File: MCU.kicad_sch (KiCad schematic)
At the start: 41 parts, among them IC9 ATSAMD21G18A-MF, J10 SAMTEC_SSW-106-01-L-S, J7 SAMTEC_SSW-108-01-G-S, J8 SAMTEC_SSW-110-01-G-S, J9 SAMTEC_SSW-108-01-G-S, Q1 XTAL_32.768KHZ_ABRACON_ABS09-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

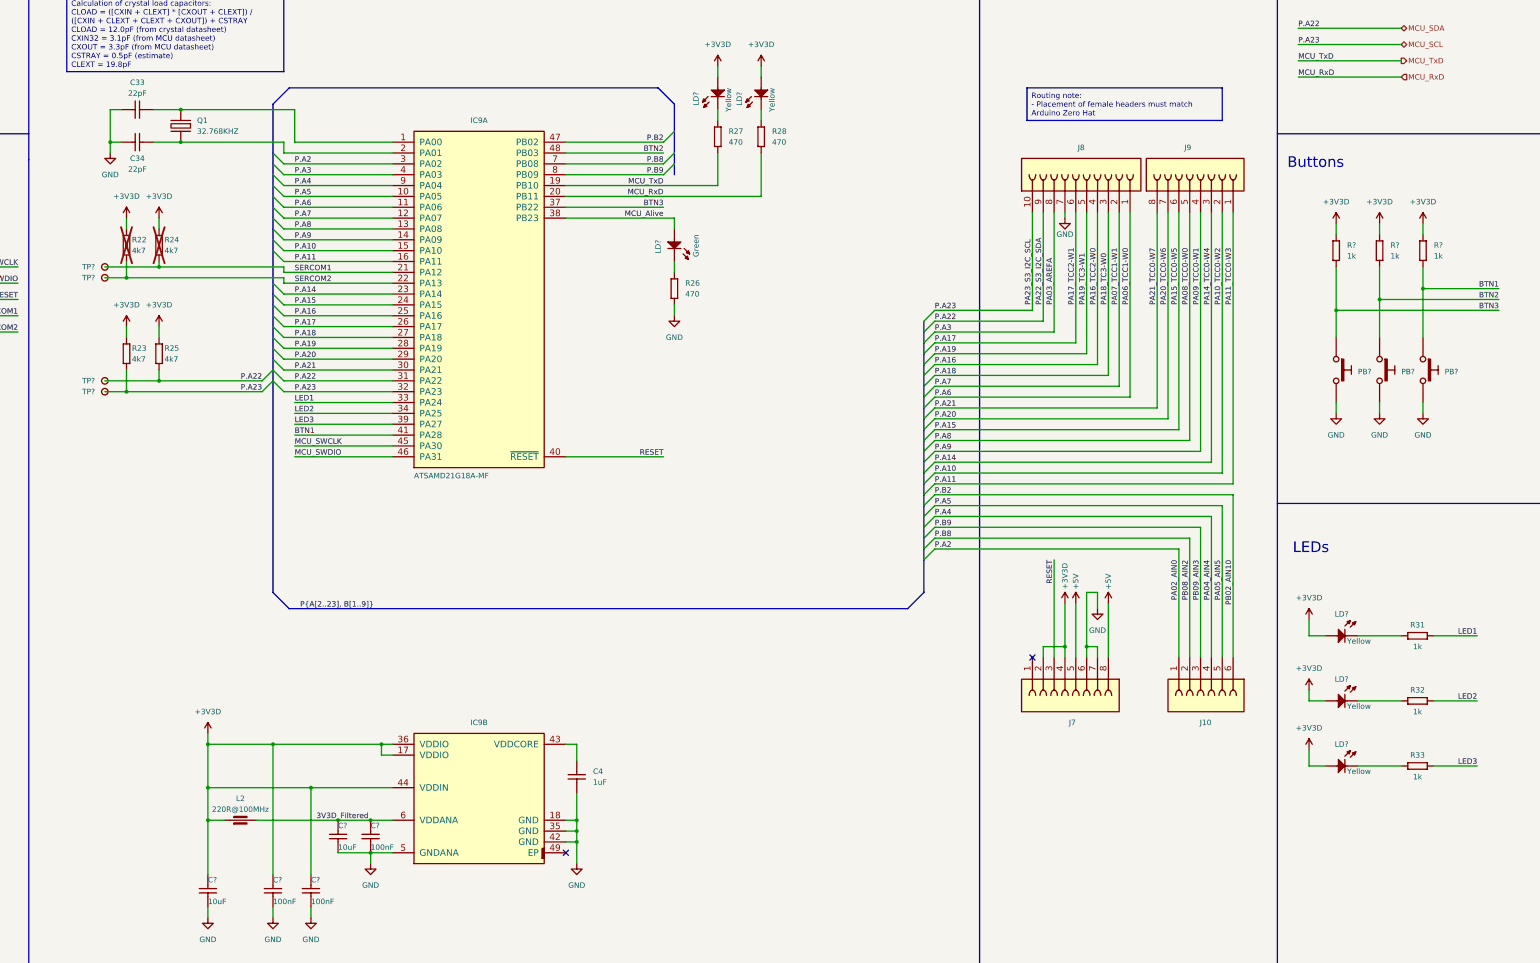
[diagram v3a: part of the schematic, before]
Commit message: Updated schematic after routing, added layout
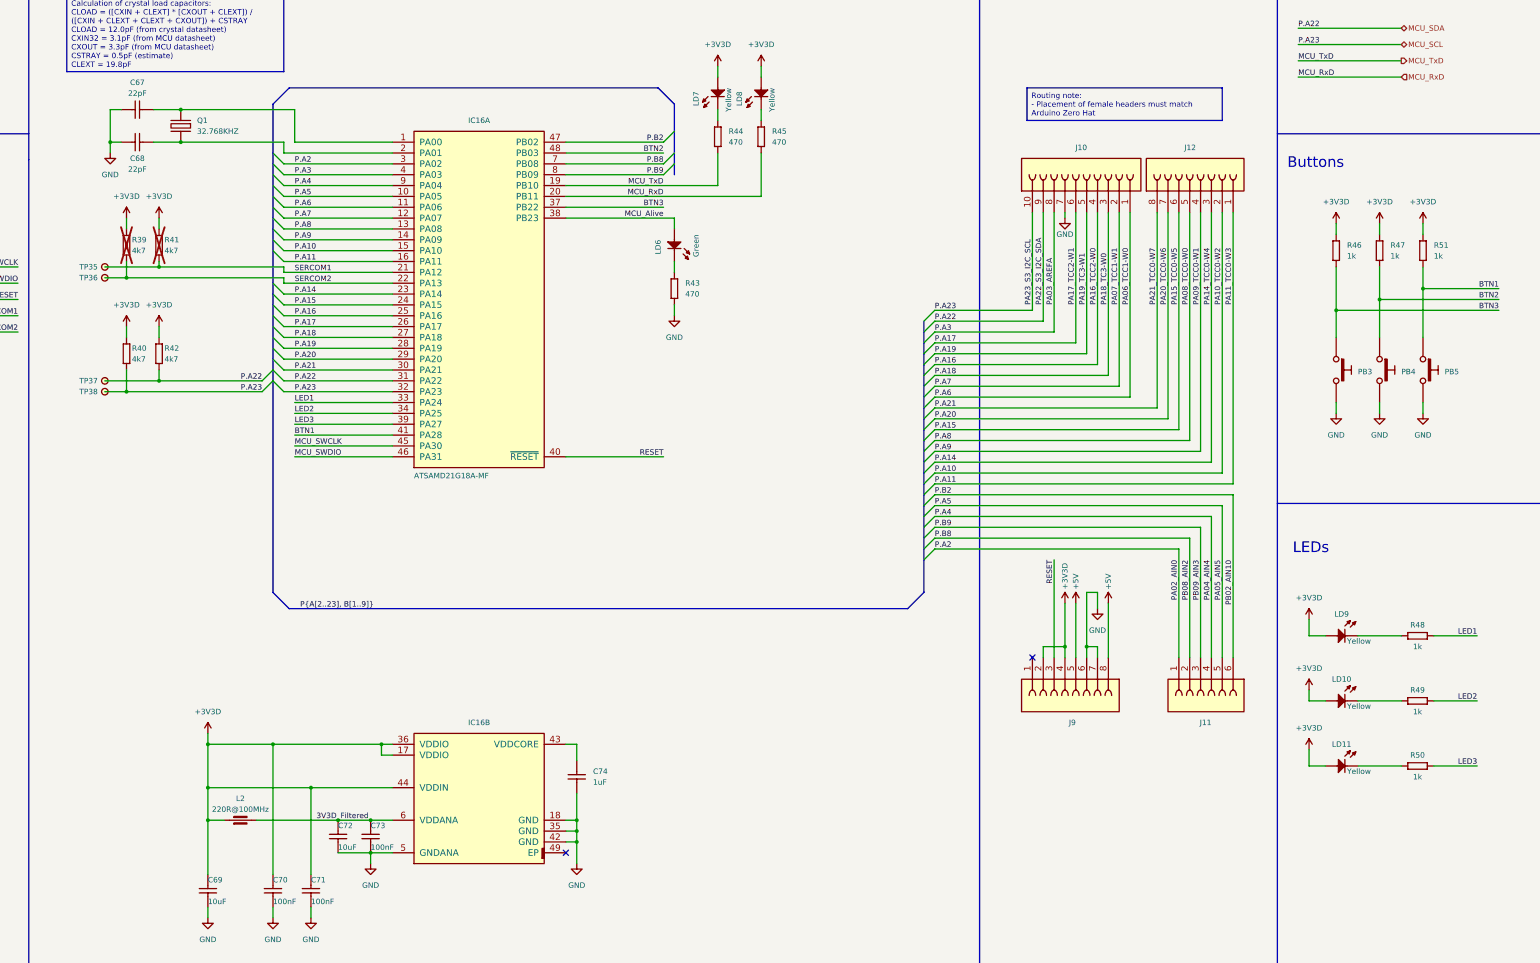
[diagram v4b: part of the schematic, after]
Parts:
- removed C33, C34: CC0603_22PF_50V_5%_NP0, Capacitors SMD:CAPC1608X87N, symbol Capacitors SMD:CC0603_22PF_50V_5%_NP0
- removed C4: CC0603_1UF_25V_10%_X7R, Capacitors SMD:CAPC1608X87N, symbol Capacitors SMD:CC0603_1UF_25V_10%_X7R
- removed C? (x3): CC0603_100NF_50V_10%_X7R, Capacitors SMD:CAPC1608X87N, symbol Capacitors SMD:CC0603_100NF_50V_10%_X7R
- removed C? (x2): CC0603_10UF_25V_20%_X5R, Capacitors SMD:CAPC1709X100N, symbol Capacitors SMD:CC0603_10UF_25V_20%_X5R
- removed IC9: ATSAMD21G18A-MF, ICs And Semiconductors SMD:QFN50P700X700X90-49N-S525, symbol Logic:ATSAMD21G18A-MF
- removed J10: SAMTEC_SSW-106-01-L-S, SAMTEC THD:SAMTEC_SSW-106-01-L-S, symbol SAMTEC:SAMTEC_SSW-106-01-L-S
- removed J7: SAMTEC_SSW-108-01-G-S, SAMTEC THD:SAMTEC_SSW-108-01-G-S, symbol SAMTEC:SAMTEC_SSW-108-01-G-S
- removed J8: SAMTEC_SSW-110-01-G-S, SAMTEC THD:SAMTEC_SSW-110-01-X-S, symbol SAMTEC:SAMTEC_SSW-110-01-G-S
- removed LD? (x5): LED_LITEON_LTST-C193KSKT-5A, ICs And Semiconductors SMD:LED_LITEON_LTST-C193KSKT-5A, symbol LEDs & Displays:LED_LITEON_LTST-C193KSKT-5A
- removed LD?: LED_LITEON_LTST-C193KGKT-5A, ICs And Semiconductors SMD:LED_LITEON_LTST-C193KGKT-5A, symbol LEDs & Displays:LED_LITEON_LTST-C193KGKT-5A
- removed PB? (x3): PB_C&K_KSC321JLFS, Switches:PB_C&K_KSC321J, symbol Switches:PB_C&K_KSC321JLFS
- removed R22, R23, R24, R25: R0603_4K7_1%_0.1W_100PPM, Resistors SMD:RESC1608X55N, symbol Resistors SMD:R0603_4K7_1%_0.1W_100PPM
- removed R26, R27, R28: R0603_470R_1%_0.1W_100PPM, Resistors SMD:RESC1608X55N, symbol Resistors SMD:R0603_470R_1%_0.1W_100PPM
- removed R31, R32, R33, R? (x3): R0603_1K_1%_0.1W_100PPM, Resistors SMD:RESC1608X55N, symbol Resistors SMD:R0603_1K_1%_0.1W_100PPM
- removed TP? (x4): SMD_PAD_1.27X1.27MM, Pads:TPS127, symbol Pads:SMD_PAD_1.27X1.27MM
- added C67, C68: CC0603_22PF_50V_5%_NP0, Capacitors SMD:CAPC1608X87N, symbol Capacitors SMD:CC0603_22PF_50V_5%_NP0
- added C69, C72: CC0603_10UF_25V_20%_X5R, Capacitors SMD:CAPC1709X100N, symbol Capacitors SMD:CC0603_10UF_25V_20%_X5R
- added C70, C71, C73: CC0603_100NF_50V_10%_X7R, Capacitors SMD:CAPC1608X87N, symbol Capacitors SMD:CC0603_100NF_50V_10%_X7R
- added C74: CC0603_1UF_25V_10%_X7R, Capacitors SMD:CAPC1608X87N, symbol Capacitors SMD:CC0603_1UF_25V_10%_X7R
- added IC16: ATSAMD21G18A-MF, ICs And Semiconductors SMD:QFN50P700X700X90-49N-S525, symbol Logic:ATSAMD21G18A-MF
- added J10: SAMTEC_SSW-110-01-G-S, SAMTEC THD:SAMTEC_SSW-110-01-X-S, symbol SAMTEC:SAMTEC_SSW-110-01-G-S
- added J11: SAMTEC_SSW-106-01-L-S, SAMTEC THD:SAMTEC_SSW-106-01-L-S, symbol SAMTEC:SAMTEC_SSW-106-01-L-S
- added J12: SAMTEC_SSW-108-01-G-S, SAMTEC THD:SAMTEC_SSW-108-01-G-S, symbol SAMTEC:SAMTEC_SSW-108-01-G-S
- added LD10, LD11, LD7, LD8, LD9: LED_LITEON_LTST-C193KSKT-5A, ICs And Semiconductors SMD:LED_LITEON_LTST-C193KSKT-5A, symbol LEDs & Displays:LED_LITEON_LTST-C193KSKT-5A
- added LD6: LED_LITEON_LTST-C193KGKT-5A, ICs And Semiconductors SMD:LED_LITEON_LTST-C193KGKT-5A, symbol LEDs & Displays:LED_LITEON_LTST-C193KGKT-5A
- added PB3, PB4, PB5: PB_C&K_KSC321JLFS, Switches:PB_C&K_KSC321J, symbol Switches:PB_C&K_KSC321JLFS
- added R39, R40, R41, R42: R0603_4K7_1%_0.1W_100PPM, Resistors SMD:RESC1608X55N, symbol Resistors SMD:R0603_4K7_1%_0.1W_100PPM
- added R43, R44, R45: R0603_470R_1%_0.1W_100PPM, Resistors SMD:RESC1608X55N, symbol Resistors SMD:R0603_470R_1%_0.1W_100PPM
- added R46, R47, R48, R49, R50, R51: R0603_1K_1%_0.1W_100PPM, Resistors SMD:RESC1608X55N, symbol Resistors SMD:R0603_1K_1%_0.1W_100PPM
- added TP35, TP36, TP37, TP38: HARWIN_S1751-46, HARWIN SMD:HARWIN_S1751-46, symbol HARWIN:HARWIN_S1751-46
- Q1: Part Description Tolerance: ± 20ppm, Stability: ±5ppm, -40°C to +85°C, 12.5p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 -> Tolerance: ±20ppm, Stability: ±5ppm, -40°C to +85°C, 12.5pF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
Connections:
- net +3V3D: now also J9.2, J9.4, C69.1, C70.1, C71.1, IC16.17 (VDDIO), IC16.36 (VDDIO), IC16.44 (VDDIN), LD10.2 (A), LD11.2 (A), LD7.2 (A), LD8.2 (A), LD9.2 (A), R39.2, R40.2, R41.2, R42.2, R46.1, R47.1, R51.1
- net +5V: now also J9.5, J9.8
- net 3V3D_Filtered: now also C72.1, C73.1, IC16.6 (VDDANA)
- net BTN1: now also IC16.41 (PA28), PB5.1, PB5.2, R51.2
- net BTN2: now also IC16.48 (PB03), PB4.1, PB4.2, R47.2
- net BTN3: now also IC16.37 (PB22), PB3.1, PB3.2, R46.2
- net GND: now also J9.6, J9.7, C67.1, C68.1, C69.2, C70.2, C71.2, C72.2, C73.2, C74.2, IC16.18 (GND), IC16.35 (GND), IC16.42 (GND), IC16.5 (GNDANA), J10.7, PB3.3, PB3.4, PB4.3, PB4.4, PB5.3, PB5.4, R43.2
- net LED1: now also IC16.33 (PA24), R48.2
- net LED2: now also IC16.34 (PA25), R49.2
- net LED3: now also IC16.39 (PA27), R50.2
- net MCU_Alive: now also IC16.38 (PB23), LD6.2 (A)
- net MCU_RxD: now also IC16.20 (PB11), R45.2
- net MCU_SCL: now also IC16.32 (PA23), J10.10, R40.1, TP38.1
- net MCU_SDA: now also IC16.31 (PA22), J10.9, R42.1, TP37.1
- net MCU_SWCLK: now also IC16.45 (PA30)
- net MCU_SWDIO: now also IC16.46 (PA31)
- net MCU_TxD: now also IC16.19 (PB10), R44.2
- net P.A10: now also IC16.15 (PA10), J12.2; no longer J9.2
- net P.A11: now also IC16.16 (PA11), J12.1; no longer J9.1
- net P.A14: now also IC16.23 (PA14), J12.3; no longer J9.3
- net P.A15: now also IC16.24 (PA15), J12.6; no longer J9.6
- net P.A16: now also IC16.25 (PA16), J10.4
- net P.A17: now also IC16.26 (PA17), J10.6
- net P.A18: now also IC16.27 (PA18), J10.3
- net P.A19: now also IC16.28 (PA19), J10.5
- net P.A2: now also IC16.3 (PA02), J11.1
- net P.A20: now also IC16.29 (PA20), J12.7; no longer J9.7
- net P.A21: now also IC16.30 (PA21), J12.8; no longer J9.8
- net P.A3: now also IC16.4 (PA03), J10.8
- net P.A4: now also IC16.9 (PA04), J11.4
- net P.A5: now also IC16.10 (PA05), J11.5
- net P.A6: now also IC16.11 (PA06), J10.1
- net P.A7: now also IC16.12 (PA07), J10.2
- net P.A8: now also IC16.13 (PA08), J12.5; no longer J9.5
- net P.A9: now also IC16.14 (PA09), J12.4; no longer J9.4
- net P.B2: now also IC16.47 (PB02), J11.6
- net P.B8: now also IC16.7 (PB08), J11.2
- net P.B9: now also IC16.8 (PB09), J11.3
- net RESET: now also J9.3, IC16.40 (~{RESET})
- net SERCOM1: now also IC16.21 (PA12), R41.1, TP35.1
- net SERCOM2: now also IC16.22 (PA13), R39.1, TP36.1
- net at Q1.2 (OSC2): now also C67.2, IC16.1 (PA00)
- net at Q1.1 (OSC1): now also C68.2, IC16.2 (PA01)
- new net: LD7.1 (C), R44.1
- new net: LD8.1 (C), R45.1
- new net: LD6.1 (C), R43.1
- new net: LD10.1 (C), R49.1
- new net: LD9.1 (C), R48.1
- new net: C74.1, IC16.43 (VDDCORE)
- new net: LD11.1 (C), R50.1

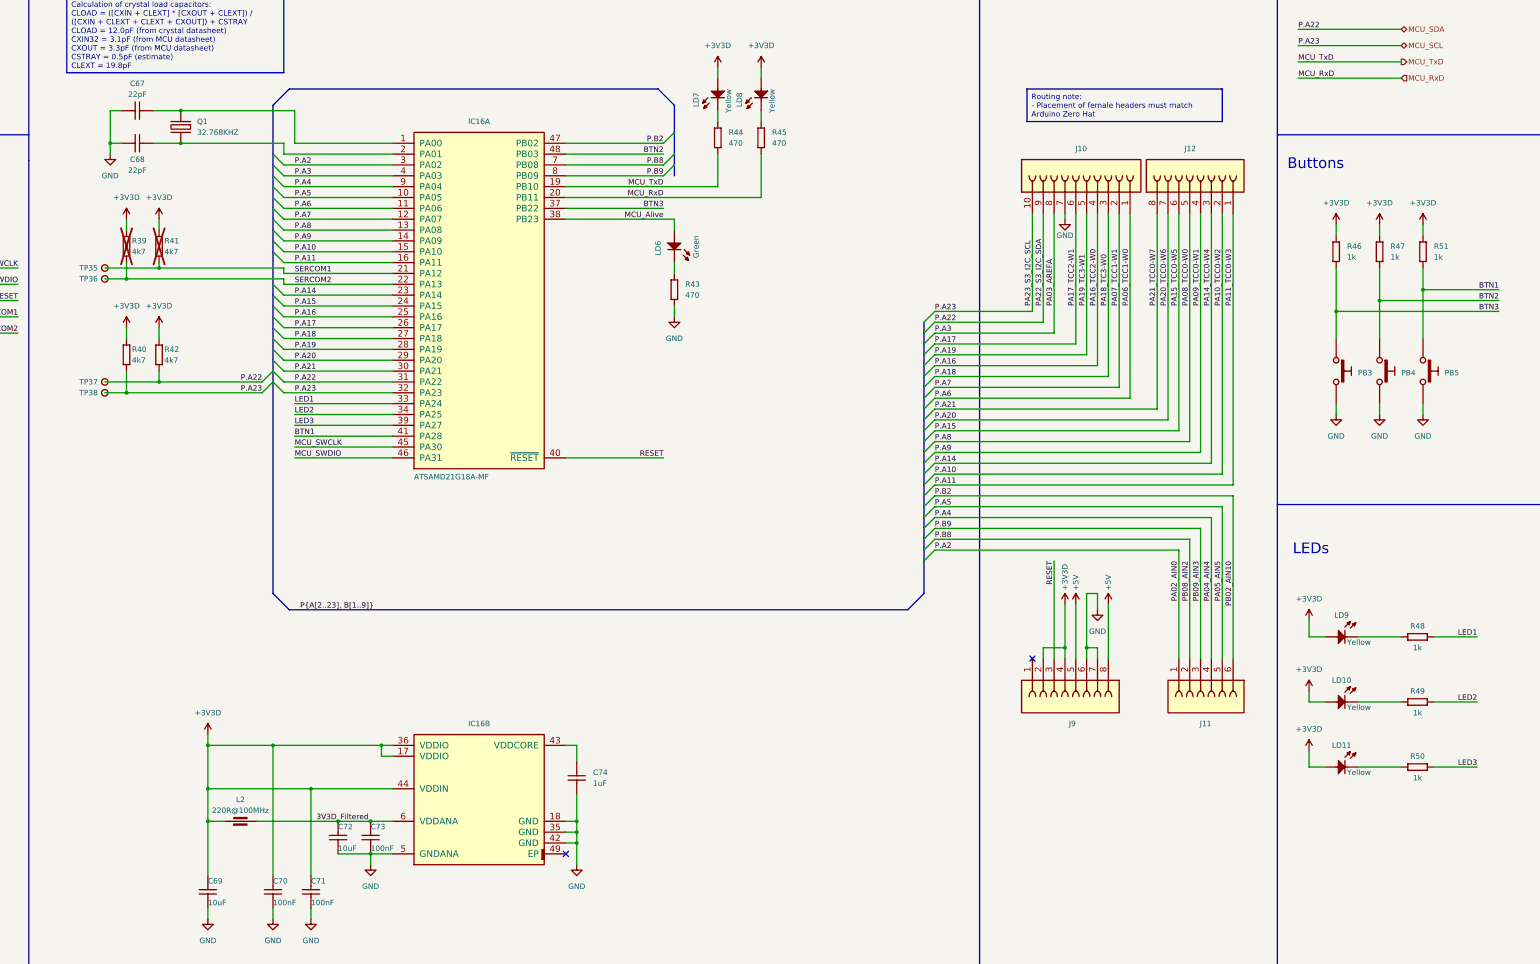
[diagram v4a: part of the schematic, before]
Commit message: Annotation now matches the produced PCB
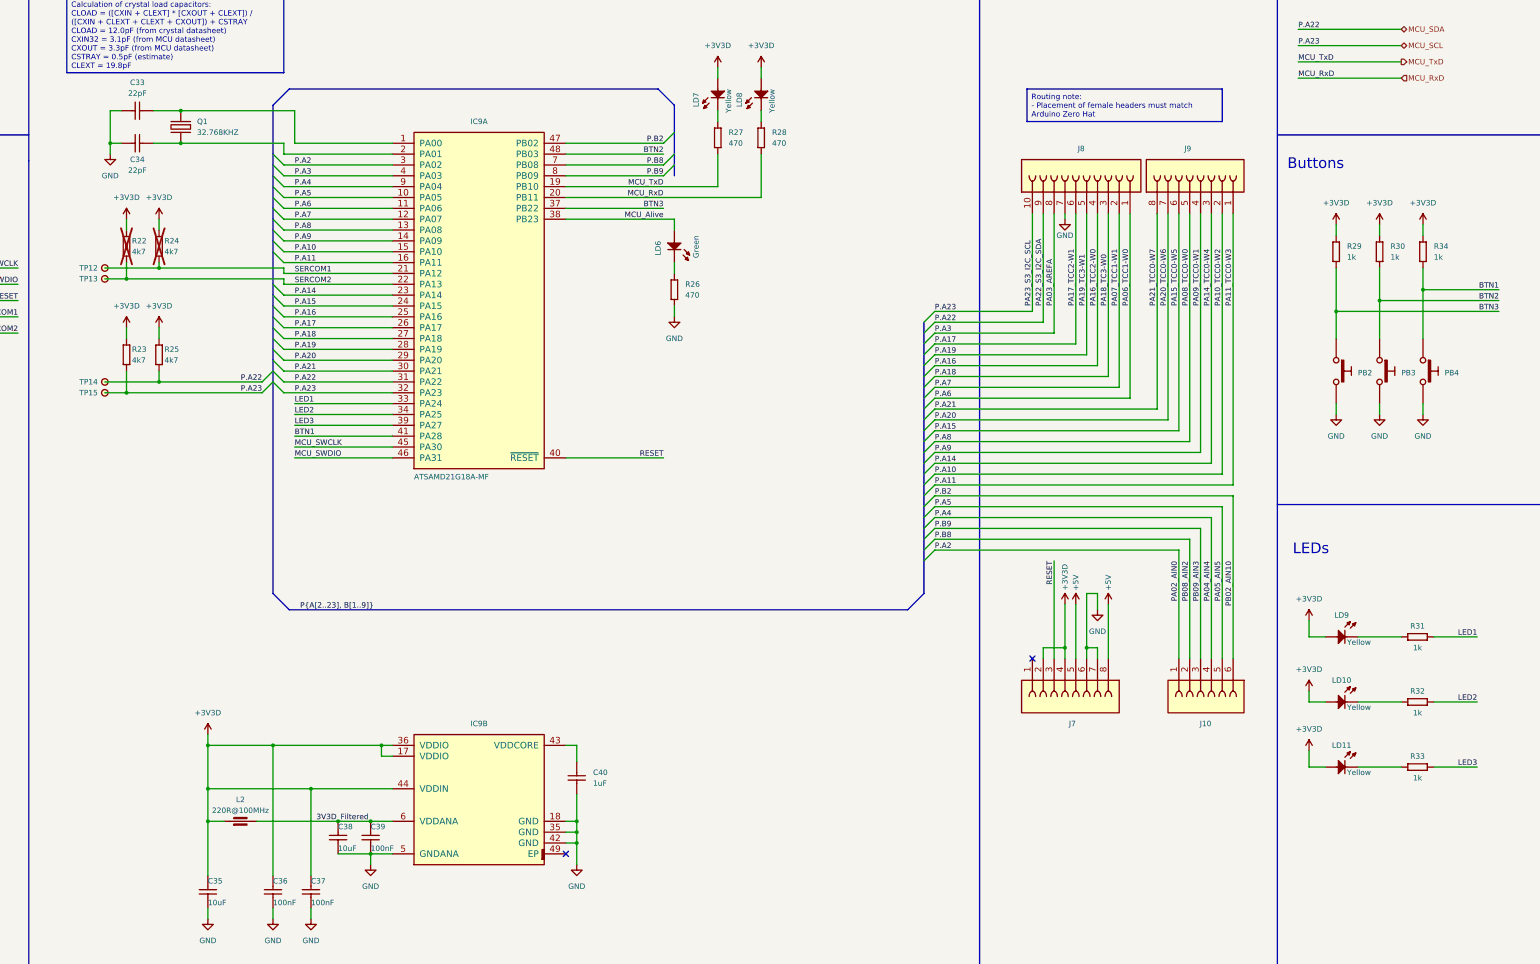
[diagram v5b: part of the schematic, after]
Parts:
- renumbered C67 to C33, C68 to C34, C69 to C35, C70 to C36, C71 to C37, C72 to C38, C73 to C39, C74 to C40, IC16 to IC9, J11 to J10, J9 to J7, J10 to J8, J12 to J9, PB3 to PB2, PB4 to PB3, PB5 to PB4, R39 to R22, R40 to R23, R41 to R24, R42 to R25, R43 to R26, R44 to R27, R45 to R28, R46 to R29, R47 to R30, R48 to R31, R49 to R32, R50 to R33, R51 to R34, TP35 to TP12, TP36 to TP13, TP37 to TP14, TP38 to TP15
